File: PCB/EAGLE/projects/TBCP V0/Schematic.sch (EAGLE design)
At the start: 29 parts, among them IC1 LM7805_TO220V, J1 12 Supply, J2 TB Header, J3 FP Header, U1 ESP32-DEVKITC, U2 TLE9201SG

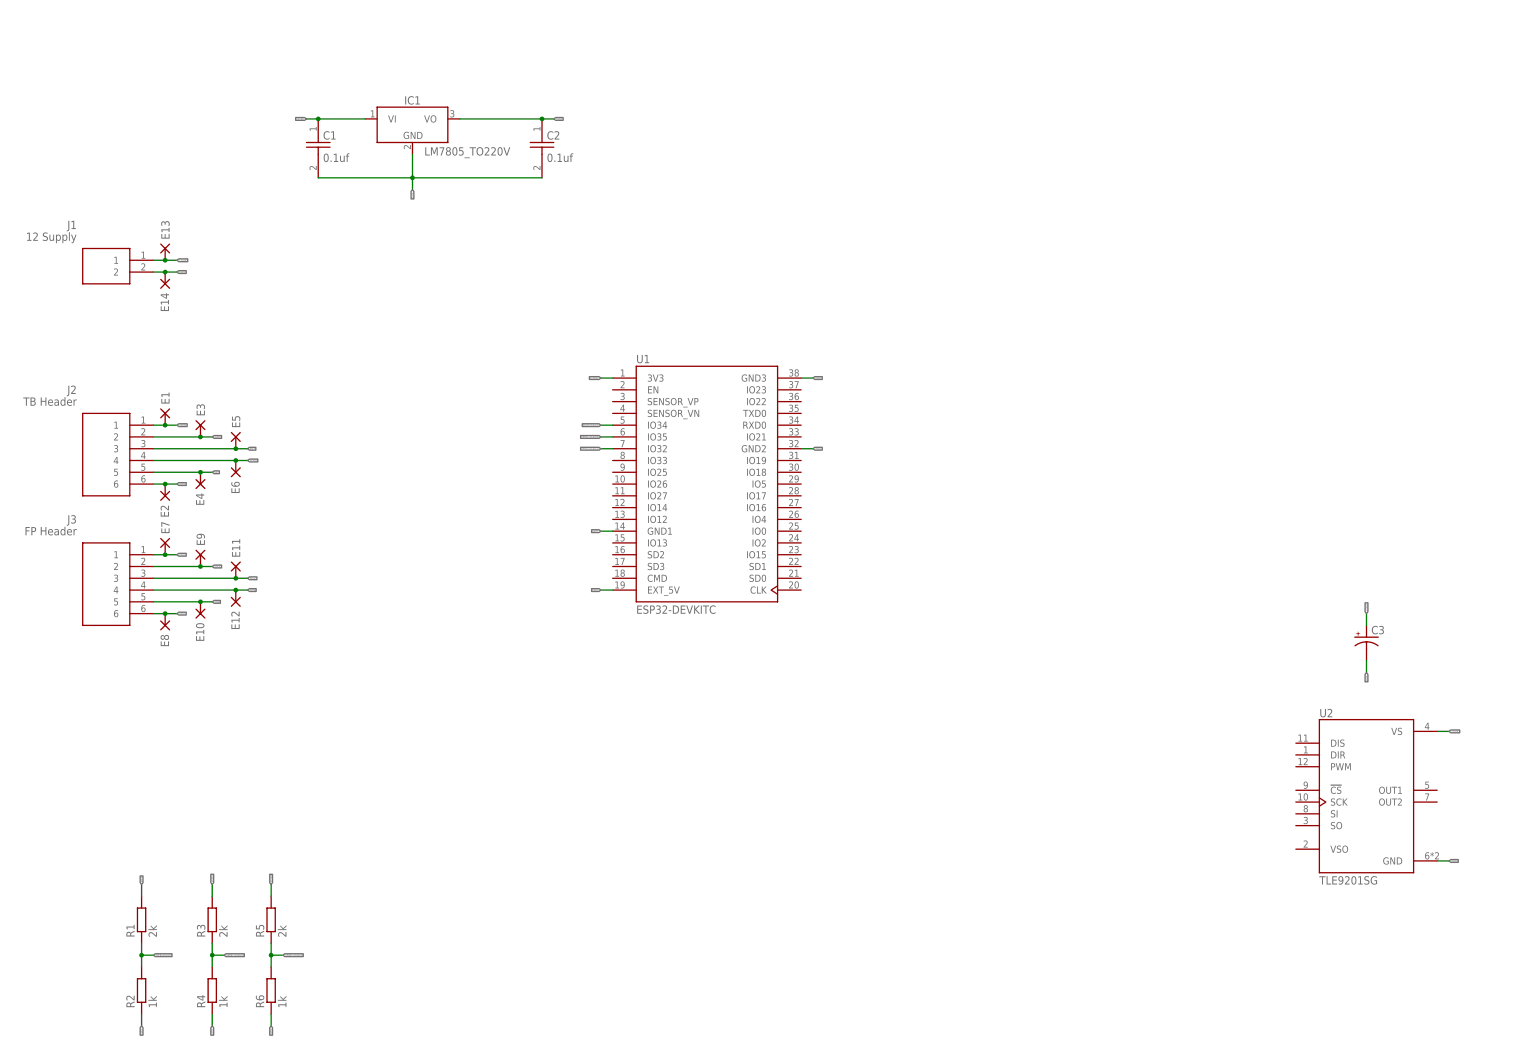
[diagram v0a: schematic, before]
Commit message: TBCP V0 - first complete PCB
All PCB traces routed and schematics ready for review
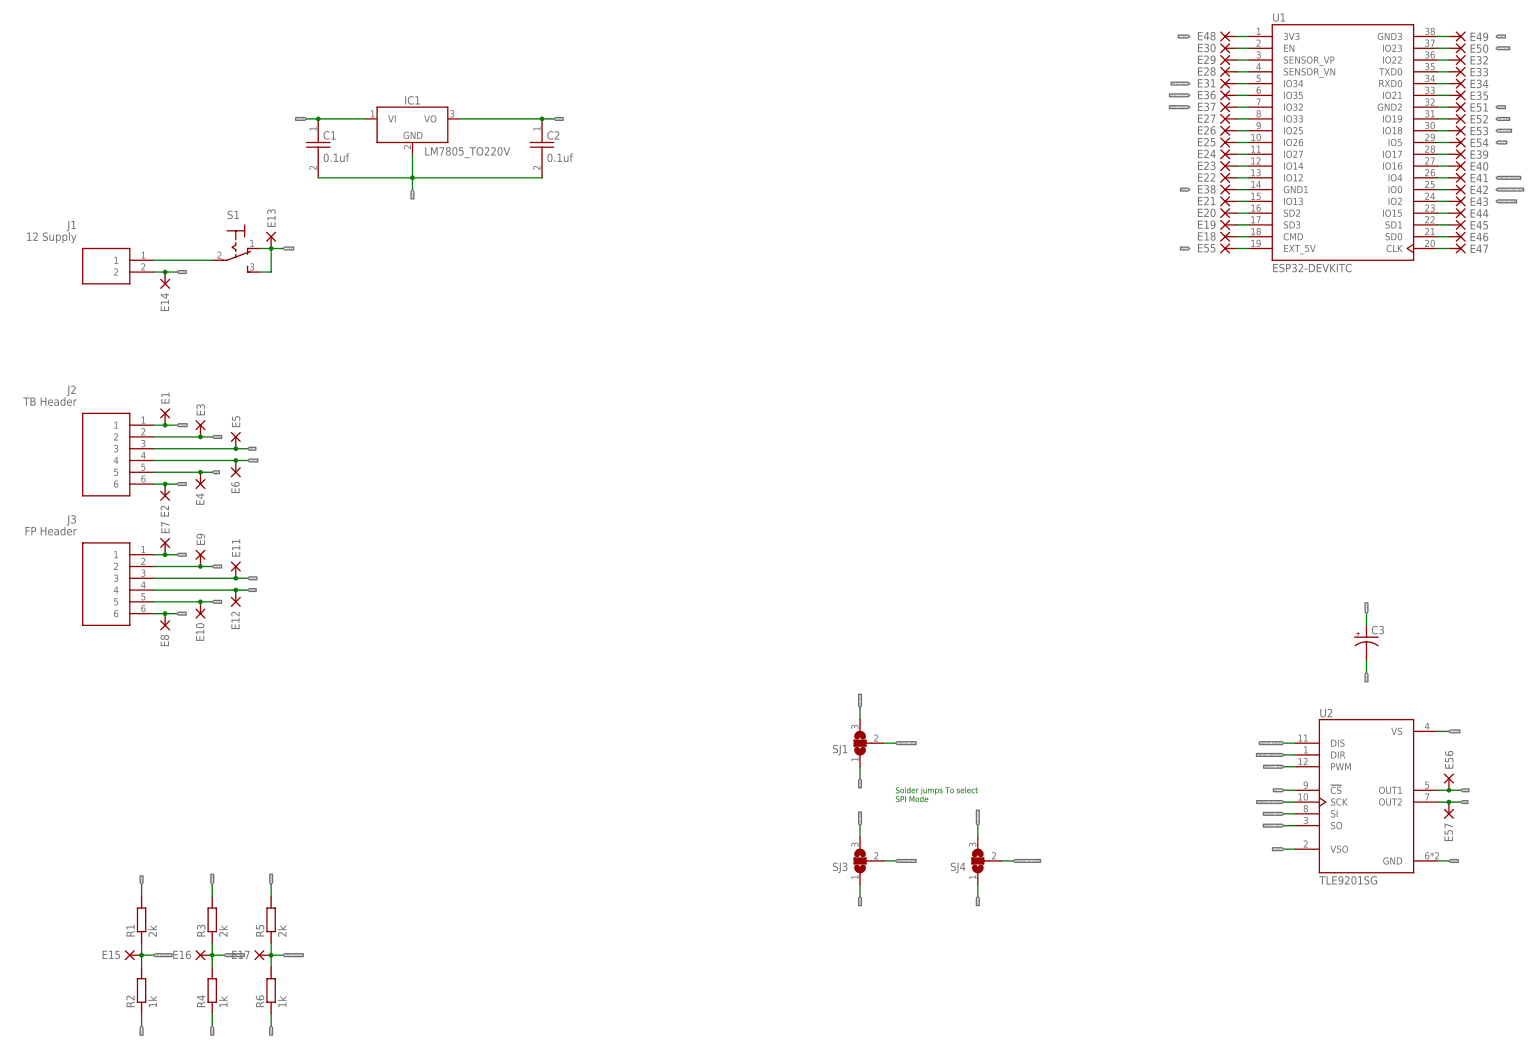
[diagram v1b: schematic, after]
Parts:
- added E15, E16, E17, E18, E19, E20, E21, E22, E23, E24, E25, E26, E27, E28, E29, E30, E31, E32, E33, E34, E35, E36, E37, E38, E39, E40, E41, E42, E43, E44, E45, E46, E47, E48, E49, E50, E51, E52, E53, E54, E55, E56, E57: DPADS_PAD-0400-S, 52101-101-REV-A_v16:DPADS_PAD-0400-S
- added S1: (no value), switch:320-916
- added SJ1: (no value), jumper:SJ2W
- added SJ3, SJ4: (no value), jumper:SJ2WW
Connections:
- removed net GND: E10.P, J3.5
- new net HBRDIGE_DISABLE: E41.P, U1.IO4
- new net HBRIDGE_DIRECTION: E42.P, U1.IO0, U2.DIR
- new net HBRIDGE_DISALBE: U2.DIS
- new net HBRIDGE_MISO: SJ3.2, U2.SO
- new net HBRIDGE_MOSI: SJ1.2, U2.SI
- new net HBRIDGE_PWM: E43.P, U1.IO2, U2.PWM
- new net HBRIDGE_SPI_CLOCK: SJ4.2, U2.SCK
- new net N$1: J1.1, S1.P
- new net N$10: E39.P, U1.IO17
- new net N$11: E40.P, U1.IO16
- new net N$15: E44.P, U1.IO15
- new net N$16: E45.P, U1.SD1
- new net N$17: E46.P, U1.SD0
- new net N$18: E47.P, U1.CLK
- new net N$19: E30.P, U1.EN
- new net N$20: E29.P, U1.SENSOR_VP
- new net N$21: E28.P, U1.SENSOR_VN
- new net N$22: E27.P, U1.IO33
- new net N$23: E26.P, U1.IO25
- new net N$24: E25.P, U1.IO26
- new net N$25: E24.P, U1.IO27
- new net N$26: E23.P, U1.IO14
- new net N$27: E22.P, U1.IO12
- new net N$28: E21.P, U1.IO13
- new net N$29: E20.P, U1.SD2
- new net N$3: E32.P, U1.IO22
- new net N$30: E19.P, U1.SD3
- new net N$31: E18.P, U1.CMD
- new net N$4: E33.P, U1.TXD0
- new net N$5: E34.P, U1.RXD0
- new net N$6: E35.P, U1.IO21
- new net N$7: S1.S
- new net SPI_CLOCK: E53.P, SJ4.3, U1.IO18
- new net SPI_CS: E54.P, U1.IO5, U2.!CS
- new net SPI_MISO: E52.P, SJ3.3, U1.IO19
- new net SPI_MOSI: E50.P, SJ1.3, U1.IO23
- net 0VDC: now also E10.P, E38.P, E49.P, E51.P, J3.5, SJ1.1, SJ3.1, SJ4.1
- net 12VDC: now also S1.O; no longer J1.1
- net 3.3VDC: now also E48.P, U2.VSO
- net 5VDC: now also E55.P
- net M0+: now also E56.P, U2.OUT1
- net M0-: now also E57.P, U2.OUT2
- net PPFB-SCALED: now also E15.P, E31.P
- net VPFB1-SCALED: now also E16.P, E37.P, U1.IO32; no longer U1.IO35
- net VPFB2-SCALED: now also E17.P, E36.P, U1.IO35; no longer U1.IO32
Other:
- note added: "Solder jumps To select SPI Mode"
- moved on the sheet: E13, U1

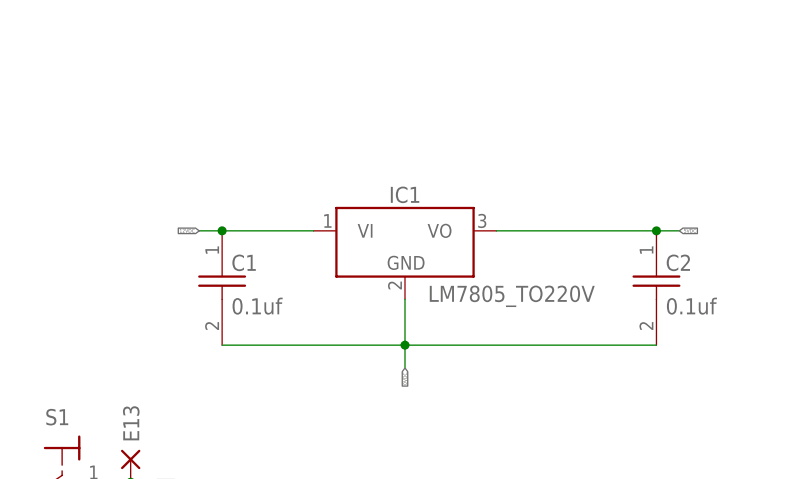
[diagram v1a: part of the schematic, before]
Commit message: Name change
Updated IC1 to U3
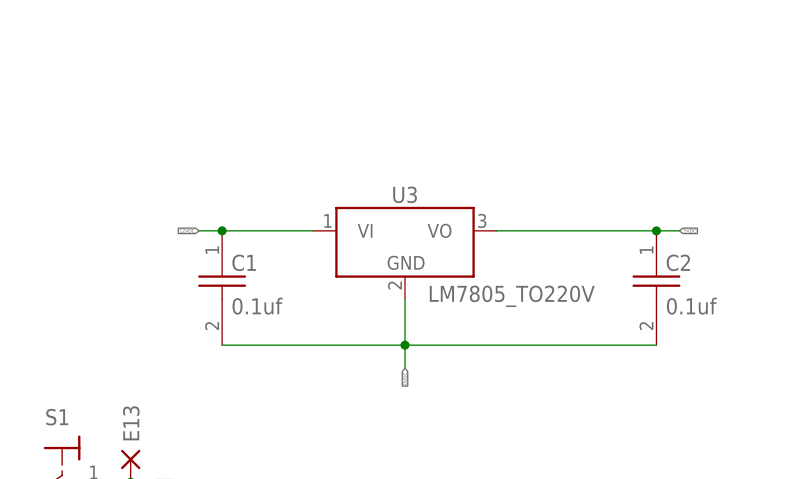
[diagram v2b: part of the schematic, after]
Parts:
- renumbered IC1 to U3
